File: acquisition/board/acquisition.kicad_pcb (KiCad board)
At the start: 6 copper layers, 103 x 90.5 mm, 432 parts, among them J1 XILINX_JTAG, J10 MMCX, J11 MMCX, J12 MMCX, J13 MMCX, J14 MMCX, J15 MMCX, J16 MMCX, J17 MMCX, J18 UX60SX-MB-5ST, J19 CONN_01X05, J2 MMCX, J20 CONN_01X06, J3 MMCX, J4 MMCX, J5 MMCX, J6 MMCX, J7 MMCX, J8 MMCX, J9 MMCX, Q1 SSM6N58NU, Q2 SSM6N58NU, U1 AD9251, U10 FT232HL, U11 LMK04806, U12 AK5DAF1-100.0000T2, U14 74AVCH1T45, U15 74AVCH1T45, U16 74AVCH1T45, U17 74AVCH1T45, U18 74AVCH1T45, U19 74AVCH1T45, U2 XC7A50T-1FTG256C, U20 74AVCH1T45, U21 ECS-3225MVQ-120-CN-TR, U22 93LC56B-MS, U23 74AVCH1T45, U24 74AVCH1T45, U25 LTC3374-QFN, U26 LT3042, U27 LT3042, U28 ADR510, U29 SIP32408, U3 AD9251, U30 LDO1117-12, U4 AD9251, U5 AD9251, U6 ICE40UP5K_QFN48, U7 STM32L031-QFN32, U8 S27KS0642, U9 S25FL128SAGBHIA10

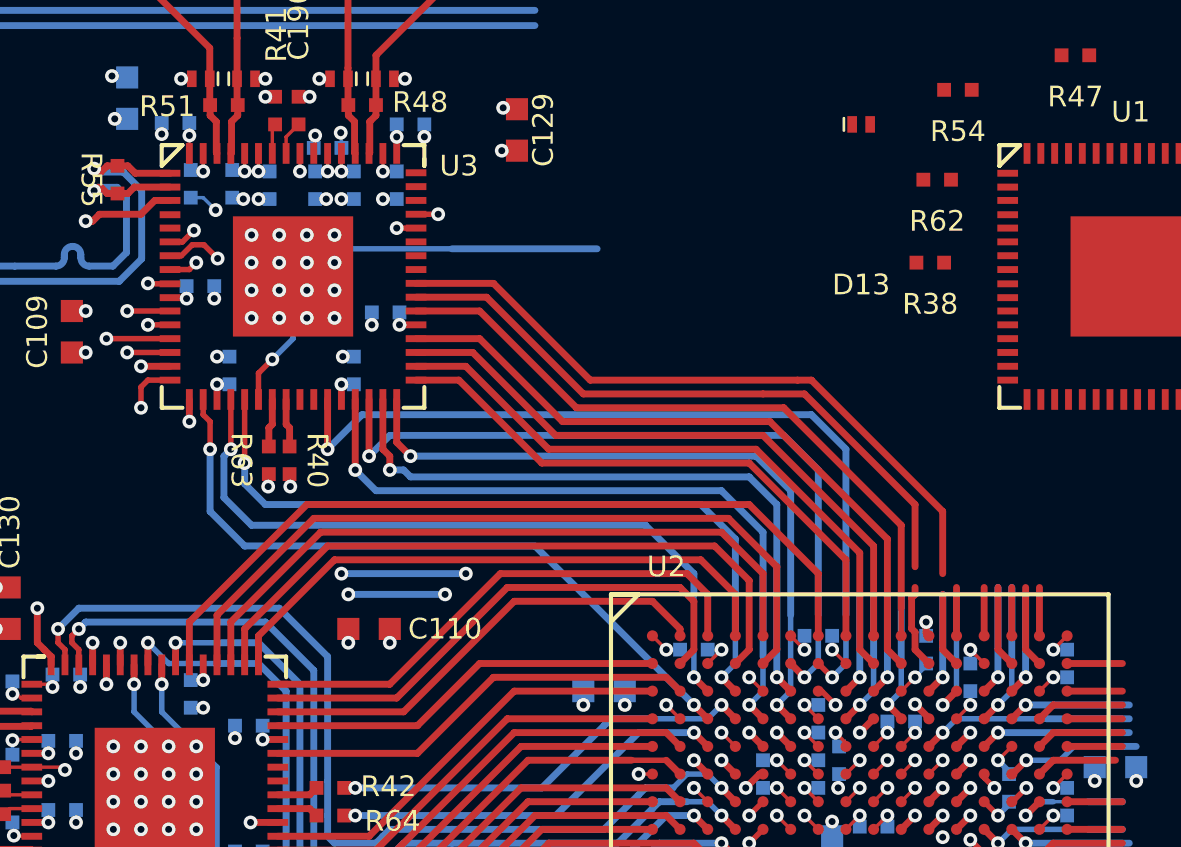
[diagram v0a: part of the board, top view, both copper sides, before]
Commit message: Fully routed ADC #3
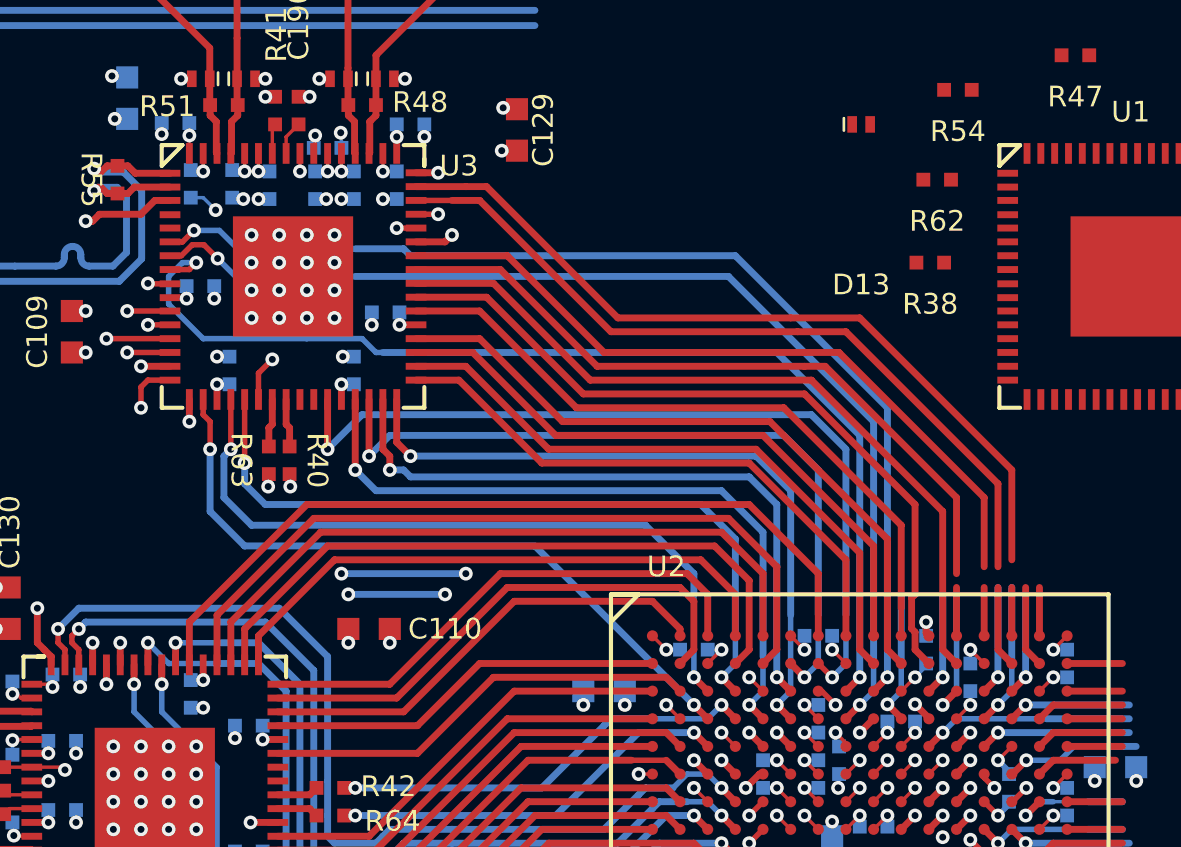
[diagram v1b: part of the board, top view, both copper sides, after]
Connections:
- U2 pad B11: /ADCs/D0_8 -> /ADCs/D2_10
- U2 pad B12: /ADCs/D0_9 -> /ADCs/D2_11
- U2 pad B14: /ADCs/D5_1 -> /ADCs/D0_11
- U2 pad C12: /ADCs/D5_2 -> /ADCs/D0_1
- U2 pad C14: /ADCs/D5_0 -> /ADCs/D0_2
- U2 pad C8: /ADCs/D0_1 -> /ADCs/D5_2
- U2 pad C9: /ADCs/D0_2 -> /ADCs/D5_0
- U2 pad D8: /ADCs/D0_11 -> /ADCs/D5_1
- U2 pad E16: /ADCs/D2_11 -> /ADCs/D0_9
- U2 pad F13: /ADCs/D2_10 -> /ADCs/D0_8
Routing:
- net /ADCs/CLIP_2: track 0.00 -> 34.1 mm, vias 0 -> 1
- net /ADCs/ADC1_OE_N: track 1.75 -> 30.8 mm
- net /ADCs/ADC1_CS_N: track 3.96 -> 32.3 mm
- net /ADCs/D2_13: track 2.96 -> 29.6 mm
- net /ADCs/D2_12: track 2.00 -> 27.7 mm
- net /ADCs/CLIP_5: track 16.8 -> 39.8 mm
- net /ADCs/D5_0: track 18.4 -> 39.2 mm
- net /ADCs/D5_1: track 19.2 -> 39.4 mm, vias 1 -> 2
- net /ADCs/D5_2: track 29.6 -> 39.7 mm
- net /ADCs/D0_1: track 3.71 -> 12.6 mm
- net /VREF: track 114.4 -> 122.0 mm
- net /ADCs/ADC_SDIO: track 122.0 -> 129.2 mm
- net /MCU/ADC1_PDWN: track 0.00 -> 5.55 mm, vias 0 -> 1
- net /ADCs/ADC_SCLK: track 130.9 -> 136.4 mm
- net /ADCs/D0_8: track 3.06 -> 7.56 mm, vias 0 -> 1
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
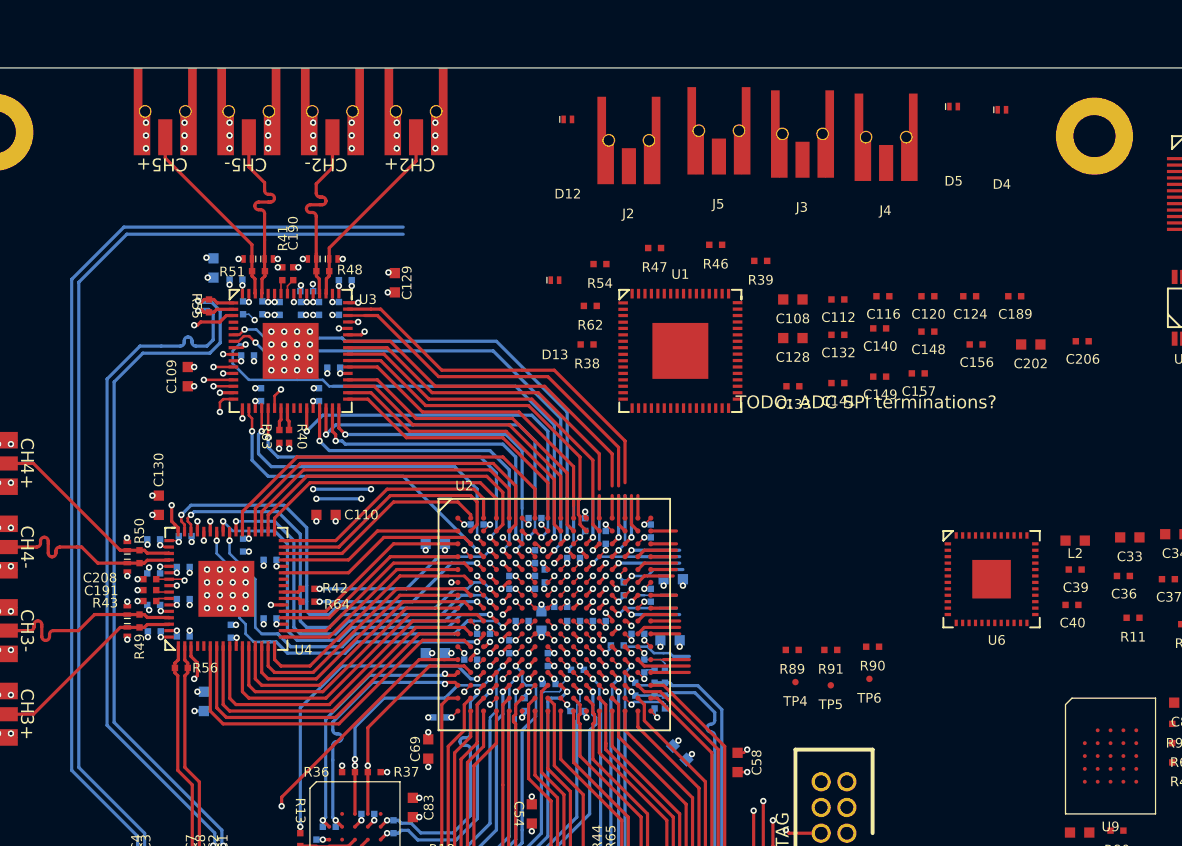
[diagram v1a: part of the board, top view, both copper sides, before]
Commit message: Initial placement and power/clock routing for fourth ADC
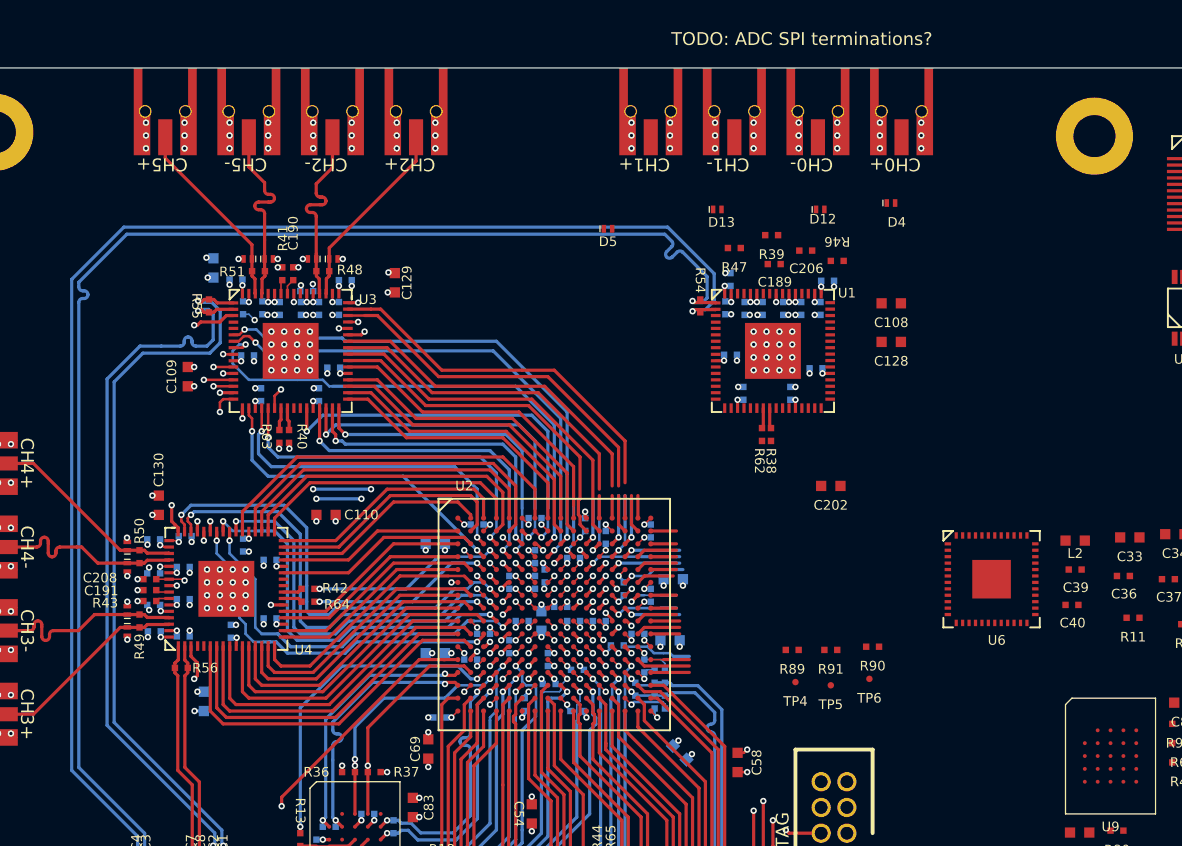
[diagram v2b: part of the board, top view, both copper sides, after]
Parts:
- C112, C116, C120, C124, C132, C133, C140, C141, C148, C149, C156, C157: moved to B.Cu
- moved D5 28.5 mm to (88.7, 37.5)
- moved C206 22.6 mm to (104.0, 39.2)
- moved J2 21.3 mm to (111.5, 31.8)
- moved D12 20.8 mm to (105.2, 36.0)
- moved C156 19.7 mm to (97.8, 43.6), turned to -90 degrees
- moved C124 19.1 mm to (98.2, 47.3)
- moved C202 19.0 mm to (106.0, 57.5)
- moved C189 18.9 mm to (101.6, 40.2)
- moved J4 18.4 mm to (92.0, 31.8)
- moved R62 16.7 mm to (100.7, 53.5), turned to -90 degrees
- moved R38 15.9 mm to (101.3, 53.5), turned to -90 degrees
- moved D13 13.8 mm to (97.2, 36.0)
- moved C141 11.6 mm to (98.2, 41.4), turned to -90 degrees
- moved D4 11.3 mm to (110.7, 35.5)
- moved C116 10.4 mm to (102.8, 50.3), turned to 90 degrees
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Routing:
- net /GND: track 936.8 -> 1077.9 mm, vias 291 -> 343
- net /ADCs/A1V8_1: track 19.8 -> 61.2 mm, vias 10 -> 19
- net /ADCs/CLK0_P: track 73.8 -> 106.2 mm, vias 1 -> 2
- net /ADCs/CLK0_N: track 74.7 -> 106.4 mm, vias 1 -> 2
- net /D1V8: track 430.9 -> 457.7 mm, vias 63 -> 67
- net Net-(R62-Pad1): track 0.00 -> 1.59 mm
- net Net-(R38-Pad1): track 0.00 -> 1.59 mm
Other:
- board text added: "CH0+"
- board text added: "CH0-"
- board text added: "CH1+"
- board text added: "CH1-"
